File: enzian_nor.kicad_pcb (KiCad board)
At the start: 4 copper layers, 75 x 60 mm, 30 parts, among them IC1 L7809ABD2T-TR, J1 ASP-134488-01, U1 MT35XU02GCBA1G12-0AUT

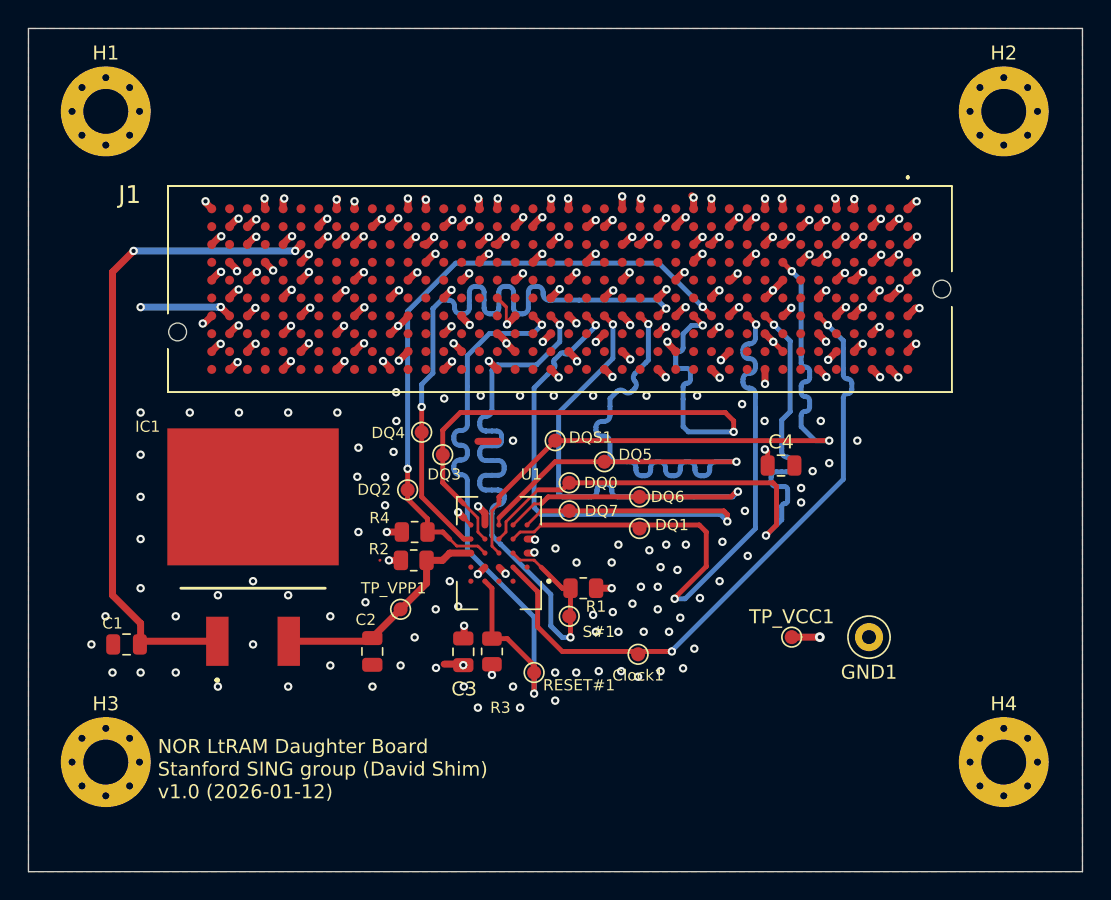
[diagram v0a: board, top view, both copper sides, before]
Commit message: Modified changes to print PCB
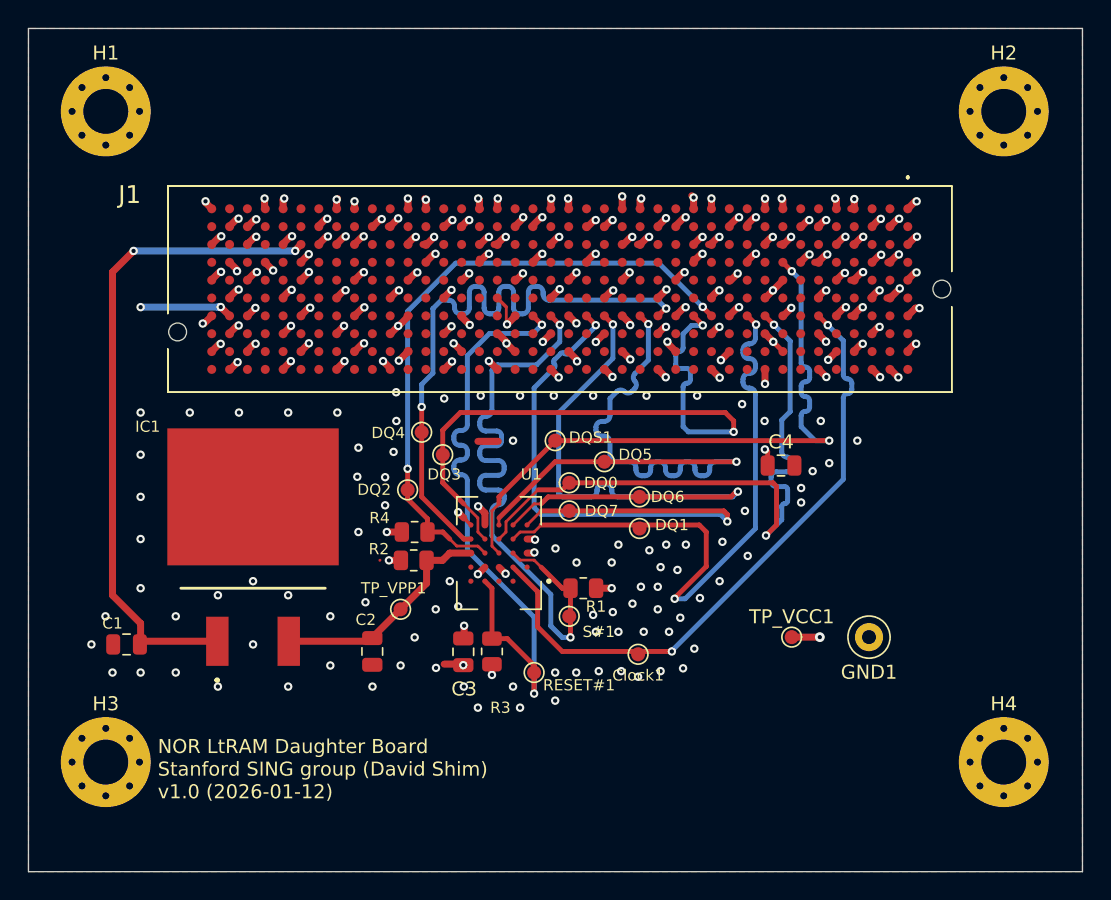
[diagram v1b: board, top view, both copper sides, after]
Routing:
- net GND: track 133.2 -> 132.2 mm
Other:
- rule pad_to_mask_clearance: 0.1 -> 0

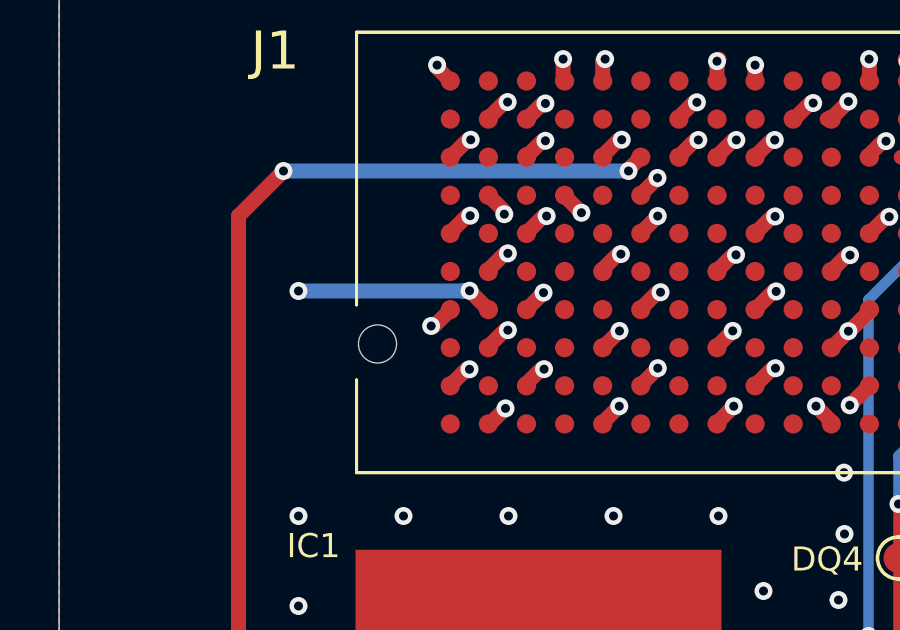
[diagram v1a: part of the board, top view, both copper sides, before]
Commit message: Added all 1V8 power pins to schematic and PCB
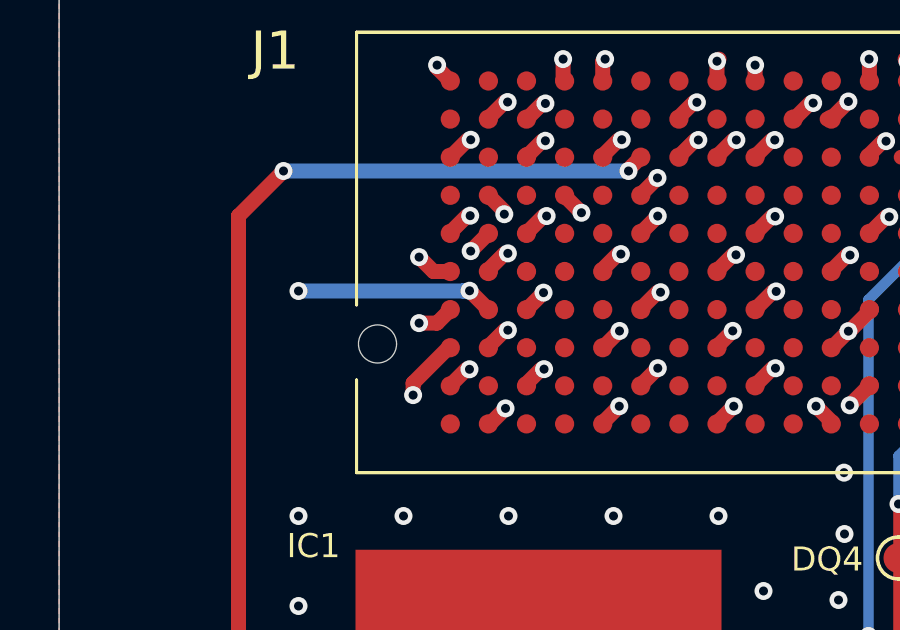
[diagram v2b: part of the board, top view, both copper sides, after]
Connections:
- J1 pad E39: unconnected-(J1-PadE39) -> VCC
- J1 pad F40: unconnected-(J1-PadF40) -> VCC
- J1 pad H40: unconnected-(J1-PadH40) -> VCC
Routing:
- net VCC: track 16.5 -> 20.6 mm, vias 11 -> 14
